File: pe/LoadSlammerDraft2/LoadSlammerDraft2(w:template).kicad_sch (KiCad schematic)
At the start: 23 parts, among them J1 Screw_Terminal_01x02, J2 Conn_Coaxial, J3 Conn_Coaxial, Q1 Q_NMOS_GDS, U1 UCC27511ADBV, U2 BD50FC0FP

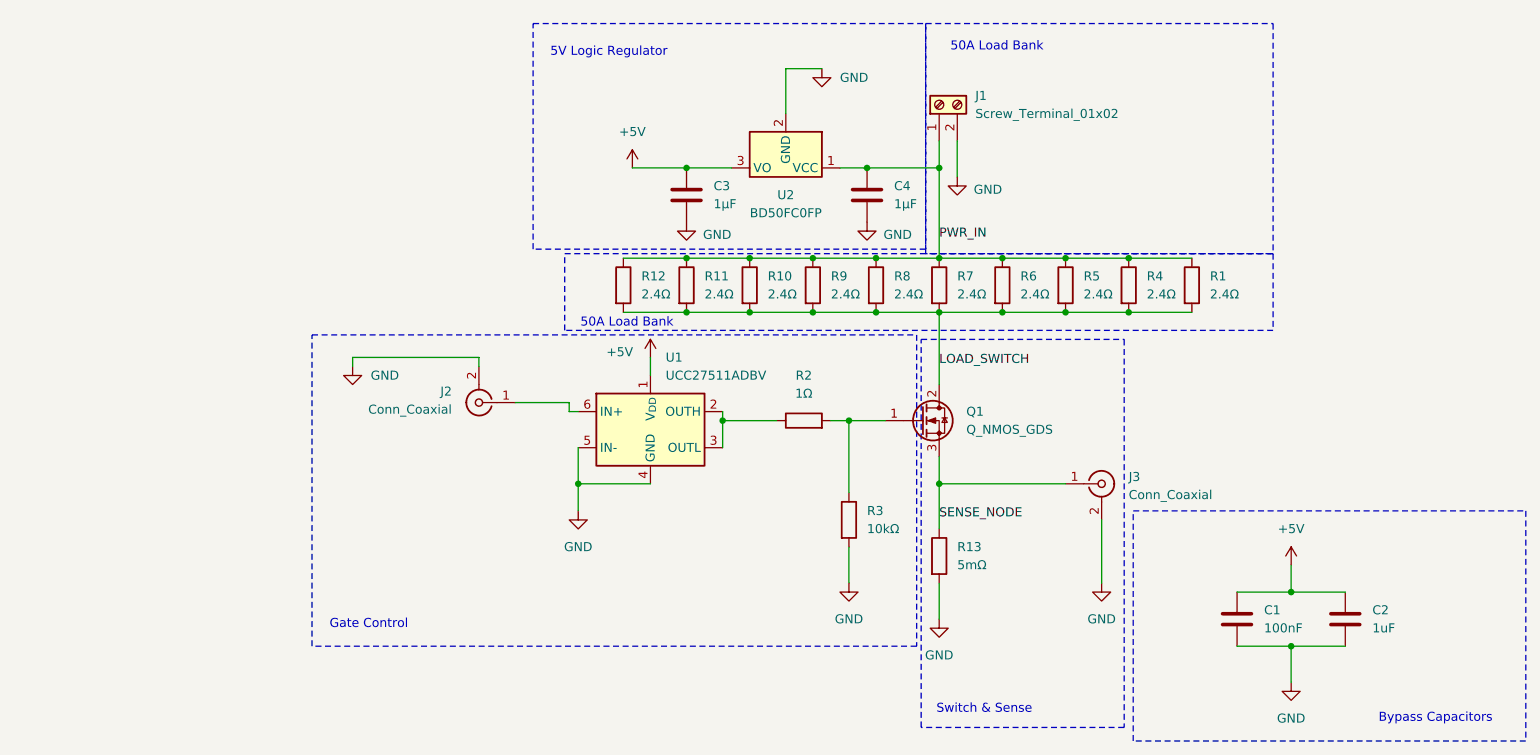
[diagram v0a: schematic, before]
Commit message: Load Slammer changes, opamp, less resistors, following template, and more
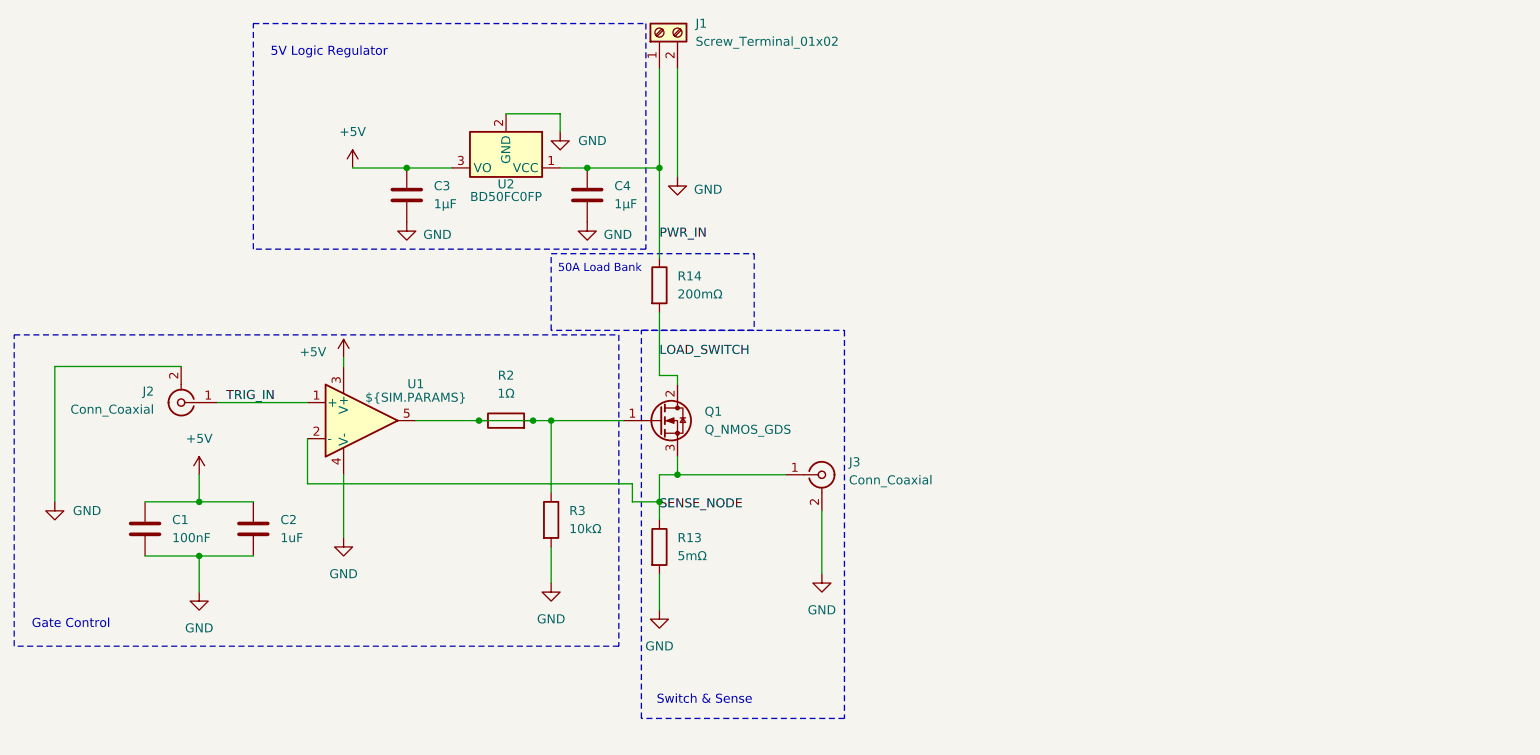
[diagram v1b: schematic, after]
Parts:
- removed R1, R10, R11, R12, R4, R5, R6, R7, R8, R9: 2.4Ω, symbol Device:R
- removed U1: UCC27511ADBV, Package_TO_SOT_SMD:SOT-23-6, symbol Driver_FET:UCC27511ADBV
- added R14: 200mΩ, Package_TO_SOT_THT:TO-247-2_Horizontal_TabDown, symbol Device:R
- added U1: ${SIM.PARAMS}, Package_TO_SOT_SMD:SOT-353_SC-70-5, symbol Simulation_SPICE:OPAMP
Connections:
- net +5V: now also U1.3 (V+)
- net GND: now also U1.4 (V-)
- net LOAD_SWITCH: now also R14.2
- net PWR_IN: now also R14.1
- net SENSE_NODE: now also U1.2 (-)
- net TRIG_IN: now reaches J2.1 (In)
- net TRIG_IN: now also U1.1 (+)
- net at R2.1: now also Q1.1 (G), R2.2, R3.1, U1.5
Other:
- note removed: "Bypass Capacitors"
- moved on the sheet: C1, C2, C3, C4, J1, J2, J3, Q1, R13, R2, R3, U2
